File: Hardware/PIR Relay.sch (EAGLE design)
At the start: 43 parts, among them J1 POWER_JACK, J2 3-PIN SMD, J4 AVR_SPI_PROG_3X22X3_LOCK, J6 RA 6Pin SMD, K1 RELAY-SPDT-JQX-15F, Q1 600mA/40V, U1 AP3012, U2 ATMEGA328P_TQFP

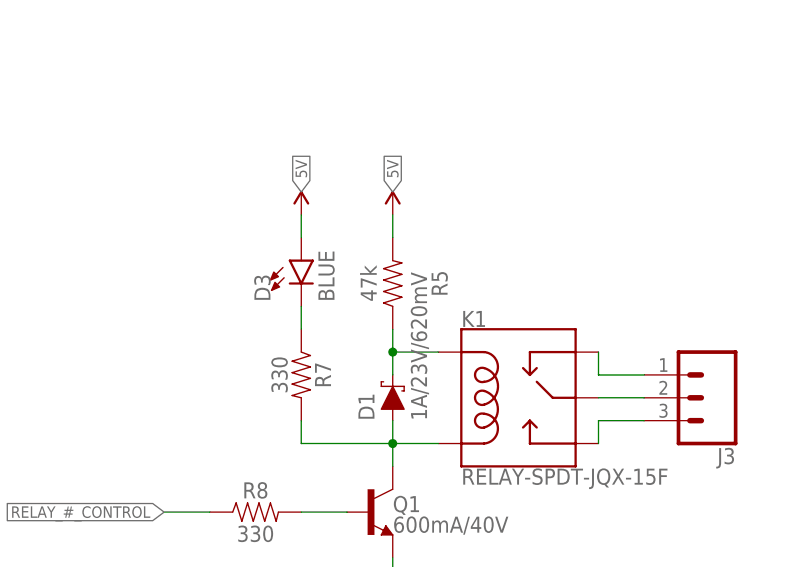
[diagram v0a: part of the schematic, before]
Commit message: swapped 47k for 0hm
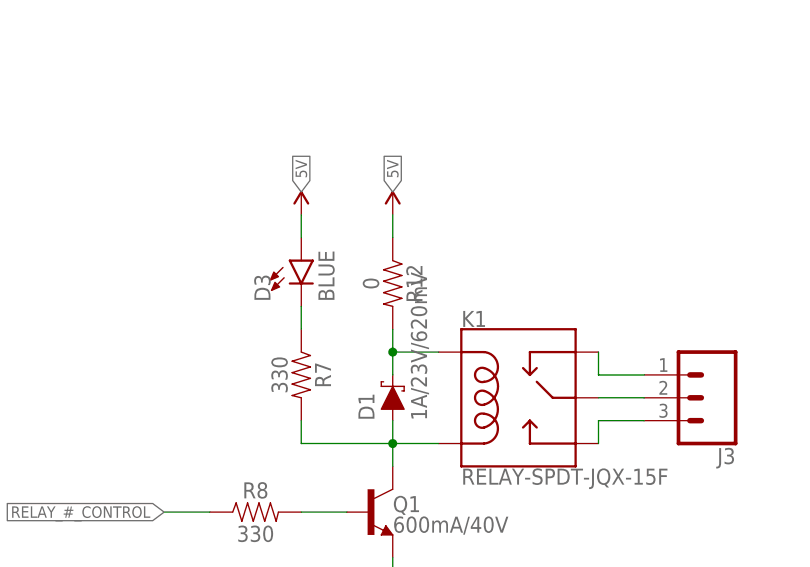
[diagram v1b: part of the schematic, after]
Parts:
- removed R5: 47k, SparkFun-Resistors:47KOHM-0603-1/10W-1%
- added R12: 0, SparkFun-Resistors:0OHM-0603-1/10W
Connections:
- net 5V: now also R12.1; no longer R5.2
- net N$8: now also R12.2; no longer R5.1
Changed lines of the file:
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@@
 <part name="K1" library="SparkFun-Electromechanical" deviceset="RELAY-SPDT" device="-JQX-15F"/>
 <part name="D3" library="SparkFun-LED" deviceset="LED-BLUE" device="0603" value="BLUE"/>
-<part name="R5" library="SparkFun-Resistors" deviceset="47KOHM" device="-0603-1/10W-1%" value="47k"/>
 <part name="R7" library="SparkFun-Resistors" deviceset="330OHM" device="-0603-1/10W-1%" value="330"/>
 <part name="R8" library="SparkFun-Resistors" deviceset="330OHM" device="-0603-1/10W-1%" value="330"/>
@@
 <part name="J6" library="SparkFun-Connectors" deviceset="CONN_06" device="SMD" value="RA 6Pin SMD"/>
 <part name="GND20" library="SparkFun-PowerSymbols" deviceset="GND" device=""/>
+<part name="R12" library="SparkFun-Resistors" deviceset="0OHM" device="-0603-1/10W" value="0"/>
 </parts>
 <sheets>
@@
 <attribute name="VALUE" x="52.705" y="86.868" size="1.778" layer="96" font="vector" rot="R90" align="top-left"/>
 </instance>
-<instance part="R5" gate="G$1" x="60.96" y="88.9" smashed="yes" rot="R90">
-<attribute name="NAME" x="67.056" y="88.9" size="1.778" layer="95" font="vector" rot="R90" align="bottom-center"/>
-<attribute name="VALUE" x="57.404" y="88.9" size="1.778" layer="96" font="vector" rot="R90" align="top-center"/>
-</instance>
 <instance part="R7" gate="G$1" x="50.8" y="78.74" smashed="yes" rot="R270">
 <attribute name="NAME" x="52.324" y="78.74" size="1.778" layer="95" font="vector" rot="R270" align="bottom-center"/>
@@
 <instance part="GND20" gate="1" x="180.34" y="144.78" smashed="yes" rot="R180">
 <attribute name="VALUE" x="180.34" y="145.034" size="1.778" layer="96" rot="R180" align="top-center"/>
+</instance>
+<instance part="R12" gate="G$1" x="60.96" y="88.9" smashed="yes" rot="R270">
+<attribute name="NAME" x="62.484" y="88.9" size="1.778" layer="95" font="vector" rot="R270" align="bottom-center"/>
+<attribute name="VALUE" x="59.436" y="88.9" size="1.778" layer="96" font="vector" rot="R270" align="top-center"/>
 </instance>
 </instances>
@@
 <segment>
 <pinref part="D1" gate="G$1" pin="C"/>
-<pinref part="R5" gate="G$1" pin="1"/>
 <wire x1="60.96" y1="78.74" x2="60.96" y2="81.28" width="0.1524" layer="91"/>
 <pinref part="K1" gate="K$1" pin="COIL1"/>
@@
 <wire x1="66.04" y1="81.28" x2="60.96" y2="81.28" width="0.1524" layer="91"/>
 <junction x="60.96" y="81.28"/>
+<pinref part="R12" gate="G$1" pin="2"/>
 </segment>
 </net>
@@
 </segment>
 <segment>
-<pinref part="R5" gate="G$1" pin="2"/>
 <pinref part="SUPPLY6" gate="G$1" pin="VCC"/>
 <wire x1="60.96" y1="93.98" x2="60.96" y2="96.52" width="0.1524" layer="91"/>
 <label x="60.96" y="99.06" size="1.27" layer="95" rot="R90" xref="yes"/>
-</segment>
-<segment>
+<pinref part="R12" gate="G$1" pin="1"/>
+</segment>
+<segment>

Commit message: v02
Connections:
- net RX renamed FTDI-RX
- net TX renamed FTDI-TX
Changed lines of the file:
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@@
 </segment>
 </net>
-<net name="TX" class="0">
+<net name="FTDI-TX" class="0">
 <segment>
 <pinref part="D6" gate="G$1" pin="A"/>
@@
 <wire x1="177.8" y1="132.08" x2="185.42" y2="132.08" width="0.1524" layer="91"/>
 <label x="185.42" y="132.08" size="1.778" layer="95"/>
-</segment>
-</net>
-<net name="RX" class="0">
-<segment>
-<pinref part="D5" gate="G$1" pin="A"/>
-<wire x1="375.92" y1="134.62" x2="375.92" y2="137.16" width="0.1524" layer="91"/>
-<label x="375.92" y="137.16" size="1.27" layer="95" rot="R90" xref="yes"/>
-</segment>
-<segment>
-<pinref part="U2" gate="U1" pin="PD1(TXD)"/>
-<wire x1="330.2" y1="152.4" x2="335.28" y2="152.4" width="0.1524" layer="91"/>
-<label x="335.28" y="152.4" size="1.27" layer="95" xref="yes"/>
-</segment>
-<segment>
-<pinref part="J6" gate="G$1" pin="2"/>
-<wire x1="177.8" y1="129.54" x2="185.42" y2="129.54" width="0.1524" layer="91"/>
-<label x="185.42" y="129.54" size="1.778" layer="95"/>
 </segment>
 </net>
@@
 </segment>
 </net>
+<net name="FTDI-RX" class="0">
+<segment>
+<pinref part="U2" gate="U1" pin="PD1(TXD)"/>
+<wire x1="330.2" y1="152.4" x2="335.28" y2="152.4" width="0.1524" layer="91"/>
+<label x="335.28" y="152.4" size="1.27" layer="95" xref="yes"/>
+</segment>
+<segment>
+<pinref part="D5" gate="G$1" pin="A"/>
+<wire x1="375.92" y1="134.62" x2="375.92" y2="137.16" width="0.1524" layer="91"/>
+<label x="375.92" y="137.16" size="1.27" layer="95" rot="R90" xref="yes"/>
+</segment>
+<segment>
+<pinref part="J6" gate="G$1" pin="2"/>
+<wire x1="177.8" y1="129.54" x2="185.42" y2="129.54" width="0.1524" layer="91"/>
+<label x="185.42" y="129.54" size="1.778" layer="95"/>
+</segment>
+</net>
